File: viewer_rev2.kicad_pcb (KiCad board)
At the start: 2 copper layers, 98 x 98 mm, 147 parts, among them J1 USB_C_Receptacle_PowerOnly_6P, Q1 DMG3414U, SW1 SW_SPDT, U1 TLC555xD

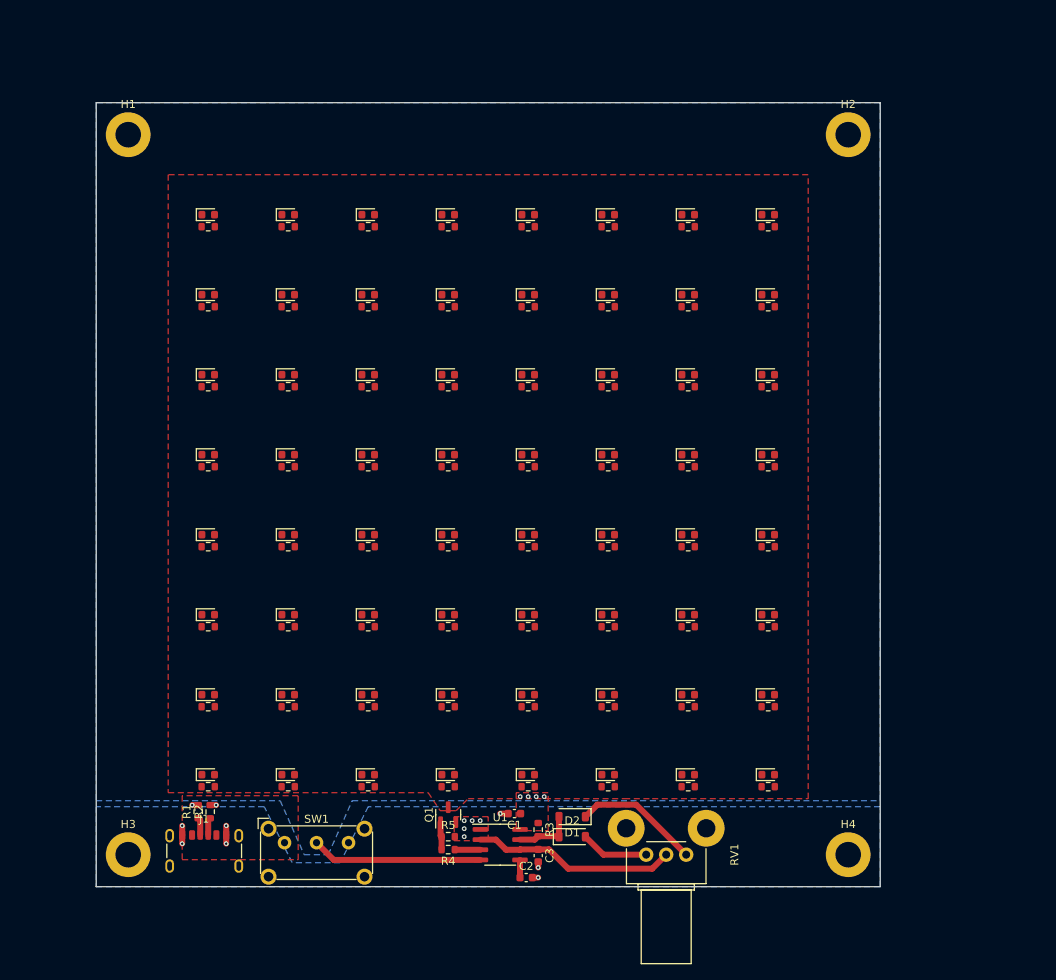
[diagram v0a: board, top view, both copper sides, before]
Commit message: Draft version for 96 well plate
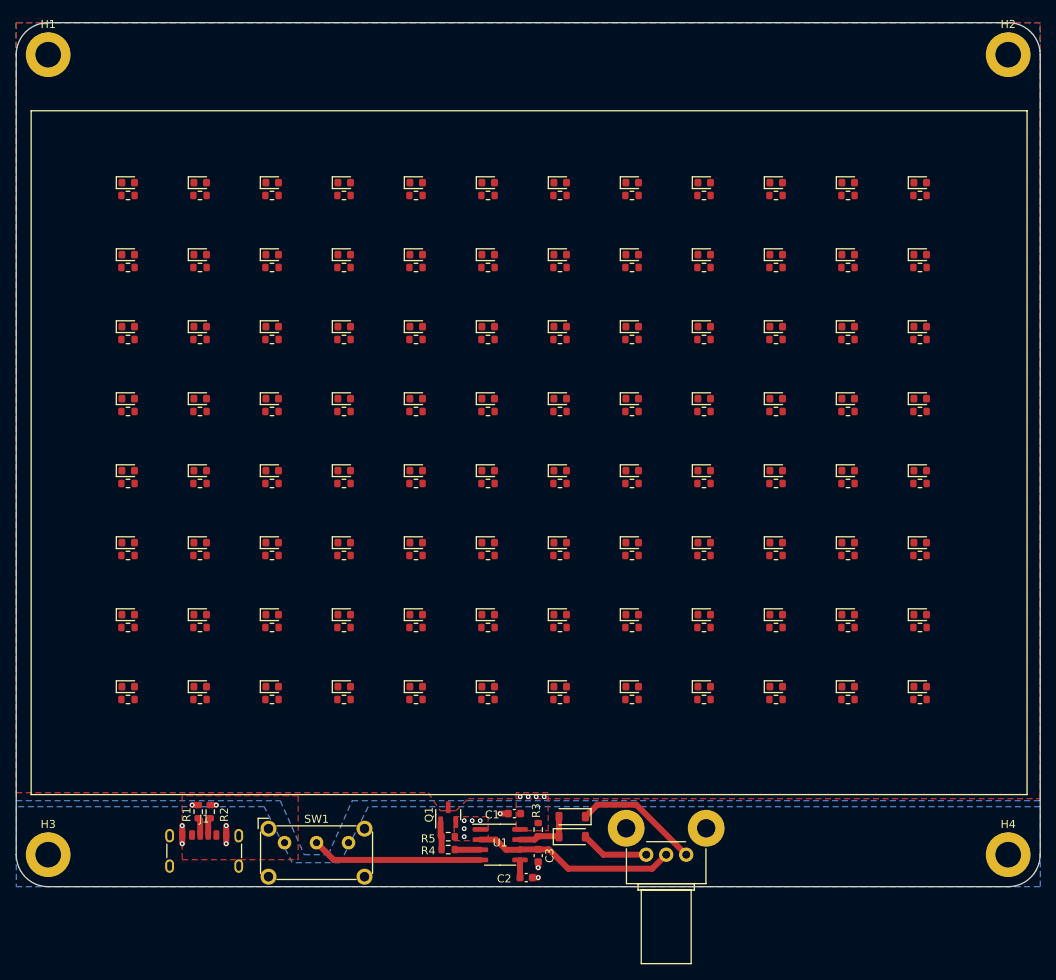
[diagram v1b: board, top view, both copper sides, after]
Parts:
- added D67: LED, LED_SMD:LED_0603_1608Metric, F.Cu at (153.5, 94.0)
- added D68: LED, LED_SMD:LED_0603_1608Metric, F.Cu at (162.5, 94.0)
- added D69: LED, LED_SMD:LED_0603_1608Metric, F.Cu at (171.5, 94.0)
- added D70: LED, LED_SMD:LED_0603_1608Metric, F.Cu at (180.5, 94.0)
- added D71: LED, LED_SMD:LED_0603_1608Metric, F.Cu at (189.5, 94.0)
- added D72: LED, LED_SMD:LED_0603_1608Metric, F.Cu at (198.5, 94.0)
- added D73: LED, LED_SMD:LED_0603_1608Metric, F.Cu at (207.5, 94.0)
- added D74: LED, LED_SMD:LED_0603_1608Metric, F.Cu at (216.5, 94.0)
- added D75: LED, LED_SMD:LED_0603_1608Metric, F.Cu at (117.5, 103.0)
- added D76: LED, LED_SMD:LED_0603_1608Metric, F.Cu at (126.5, 103.0)
- added D77: LED, LED_SMD:LED_0603_1608Metric, F.Cu at (135.5, 103.0)
- added D78: LED, LED_SMD:LED_0603_1608Metric, F.Cu at (144.5, 103.0)
- added D79: LED, LED_SMD:LED_0603_1608Metric, F.Cu at (153.5, 103.0)
- added D80: LED, LED_SMD:LED_0603_1608Metric, F.Cu at (162.5, 103.0)
- added D81: LED, LED_SMD:LED_0603_1608Metric, F.Cu at (171.5, 103.0)
- added D82: LED, LED_SMD:LED_0603_1608Metric, F.Cu at (180.5, 103.0)
- added D83: LED, LED_SMD:LED_0603_1608Metric, F.Cu at (189.5, 103.0)
- added D84: LED, LED_SMD:LED_0603_1608Metric, F.Cu at (198.5, 103.0)
- added D85: LED, LED_SMD:LED_0603_1608Metric, F.Cu at (207.5, 103.0)
- added D86: LED, LED_SMD:LED_0603_1608Metric, F.Cu at (216.5, 103.0)
- added D87: LED, LED_SMD:LED_0603_1608Metric, F.Cu at (117.5, 112.0)
- added D88: LED, LED_SMD:LED_0603_1608Metric, F.Cu at (126.5, 112.0)
- added D89: LED, LED_SMD:LED_0603_1608Metric, F.Cu at (135.5, 112.0)
- added D90: LED, LED_SMD:LED_0603_1608Metric, F.Cu at (144.5, 112.0)
- added D91: LED, LED_SMD:LED_0603_1608Metric, F.Cu at (153.5, 112.0)
- added D92: LED, LED_SMD:LED_0603_1608Metric, F.Cu at (162.5, 112.0)
- added D93: LED, LED_SMD:LED_0603_1608Metric, F.Cu at (171.5, 112.0)
- added D94: LED, LED_SMD:LED_0603_1608Metric, F.Cu at (180.5, 112.0)
- added D95: LED, LED_SMD:LED_0603_1608Metric, F.Cu at (189.5, 112.0)
- added D96: LED, LED_SMD:LED_0603_1608Metric, F.Cu at (198.5, 112.0)
- added D97: LED, LED_SMD:LED_0603_1608Metric, F.Cu at (207.5, 112.0)
- added D98: LED, LED_SMD:LED_0603_1608Metric, F.Cu at (216.5, 112.0)
- added R100: 91, Resistor_SMD:R_0603_1608Metric, F.Cu at (207.5, 113.6)
- added R101: 91, Resistor_SMD:R_0603_1608Metric, F.Cu at (216.5, 113.6)
- added R70: 91, Resistor_SMD:R_0603_1608Metric, F.Cu at (153.5, 95.6)
- added R71: 91, Resistor_SMD:R_0603_1608Metric, F.Cu at (162.5, 95.6)
- added R72: 91, Resistor_SMD:R_0603_1608Metric, F.Cu at (171.5, 95.6)
- added R73: 91, Resistor_SMD:R_0603_1608Metric, F.Cu at (180.5, 95.6)
- added R74: 91, Resistor_SMD:R_0603_1608Metric, F.Cu at (189.5, 95.6)
- added R75: 91, Resistor_SMD:R_0603_1608Metric, F.Cu at (198.5, 95.6)
- added R76: 91, Resistor_SMD:R_0603_1608Metric, F.Cu at (207.5, 95.6)
- added R77: 91, Resistor_SMD:R_0603_1608Metric, F.Cu at (216.5, 95.6)
- added R78: 91, Resistor_SMD:R_0603_1608Metric, F.Cu at (117.5, 104.6)
- added R79: 91, Resistor_SMD:R_0603_1608Metric, F.Cu at (126.5, 104.6)
- added R80: 91, Resistor_SMD:R_0603_1608Metric, F.Cu at (135.5, 104.6)
- added R81: 91, Resistor_SMD:R_0603_1608Metric, F.Cu at (144.5, 104.6)
- added R82: 91, Resistor_SMD:R_0603_1608Metric, F.Cu at (153.5, 104.6)
- added R83: 91, Resistor_SMD:R_0603_1608Metric, F.Cu at (162.5, 104.6)
- added R84: 91, Resistor_SMD:R_0603_1608Metric, F.Cu at (171.5, 104.6)
- added R85: 91, Resistor_SMD:R_0603_1608Metric, F.Cu at (180.5, 104.6)
- added R86: 91, Resistor_SMD:R_0603_1608Metric, F.Cu at (189.5, 104.6)
- added R87: 91, Resistor_SMD:R_0603_1608Metric, F.Cu at (198.5, 104.6)
- added R88: 91, Resistor_SMD:R_0603_1608Metric, F.Cu at (207.5, 104.6)
- added R89: 91, Resistor_SMD:R_0603_1608Metric, F.Cu at (216.5, 104.6)
- added R90: 91, Resistor_SMD:R_0603_1608Metric, F.Cu at (117.5, 113.6)
- added R91: 91, Resistor_SMD:R_0603_1608Metric, F.Cu at (126.5, 113.6)
- added R92: 91, Resistor_SMD:R_0603_1608Metric, F.Cu at (135.5, 113.6)
- added R93: 91, Resistor_SMD:R_0603_1608Metric, F.Cu at (144.5, 113.6)
- added R94: 91, Resistor_SMD:R_0603_1608Metric, F.Cu at (153.5, 113.6)
- added R95: 91, Resistor_SMD:R_0603_1608Metric, F.Cu at (162.5, 113.6)
- added R96: 91, Resistor_SMD:R_0603_1608Metric, F.Cu at (171.5, 113.6)
- added R97: 91, Resistor_SMD:R_0603_1608Metric, F.Cu at (180.5, 113.6)
- added R98: 91, Resistor_SMD:R_0603_1608Metric, F.Cu at (189.5, 113.6)
- added R99: 91, Resistor_SMD:R_0603_1608Metric, F.Cu at (198.5, 113.6)
- R10, R11, R12, R13, R14, R15, R16, R17, R18, R19, R20, R21, R22, R23, R24, R25, R26, R27, R28, R29, R30, R31, R32, R33, R34, R35, R36, R37, R38, R39, R40, R41, R42, R43, R44, R45, R46, R47, R48, R49, R50, R51, R52, R53, R54, R55, R56, R57, R58, R59, R6, R60, R61, R62, R63, R64, R65, R66, R67, R68, R69, R7, R8, R9: value 68 -> 91
- moved D59 72.7 mm to (189.5, 85.0)
- moved R62 72.6 mm to (189.5, 86.6)
- moved D60 71.9 mm to (198.5, 85.0)
- moved R63 71.8 mm to (198.5, 86.6)
- moved D61 71.0 mm to (207.5, 85.0)
- moved R64 70.9 mm to (207.5, 86.6)
- moved D62 70.2 mm to (216.5, 85.0)
- moved R65 70.1 mm to (216.5, 86.6)
- moved D35 67.2 mm to (189.5, 67.0)
- moved R38 67.2 mm to (189.5, 68.6)
- moved D36 66.3 mm to (198.5, 67.0)
- moved R39 66.2 mm to (198.5, 68.6)
- moved D37 65.4 mm to (207.5, 67.0)
- moved R40 65.3 mm to (207.5, 68.6)
- moved D38 64.5 mm to (216.5, 67.0)
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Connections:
- D10 pad 2: Net-(D10-A) -> Net-(D3-A)
- D11 pad 2: Net-(D11-A) -> Net-(D3-A)
- D12 pad 2: Net-(D12-A) -> Net-(D3-A)
- D13 pad 2: Net-(D13-A) -> Net-(D3-A)
- D14 pad 2: Net-(D14-A) -> Net-(D3-A)
- D15 pad 2: Net-(D15-A) -> Net-(D3-A)
- D16 pad 2: Net-(D16-A) -> Net-(D3-A)
- D17 pad 2: Net-(D17-A) -> Net-(D3-A)
- D18 pad 2: Net-(D18-A) -> Net-(D3-A)
- D19 pad 2: Net-(D19-A) -> Net-(D3-A)
- D20 pad 2: Net-(D20-A) -> Net-(D3-A)
- D21 pad 2: Net-(D21-A) -> Net-(D3-A)
- D22 pad 2: Net-(D22-A) -> Net-(D3-A)
- D23 pad 2: Net-(D23-A) -> Net-(D3-A)
- D24 pad 2: Net-(D24-A) -> Net-(D3-A)
- D25 pad 2: Net-(D25-A) -> Net-(D3-A)
- D26 pad 2: Net-(D26-A) -> Net-(D3-A)
- D27 pad 2: Net-(D27-A) -> Net-(D3-A)
- D28 pad 2: Net-(D28-A) -> Net-(D3-A)
- D29 pad 2: Net-(D29-A) -> Net-(D3-A)
- D30 pad 2: Net-(D30-A) -> Net-(D3-A)
- D31 pad 2: Net-(D31-A) -> Net-(D3-A)
- D32 pad 2: Net-(D32-A) -> Net-(D3-A)
- D33 pad 2: Net-(D33-A) -> Net-(D3-A)
- D34 pad 2: Net-(D34-A) -> Net-(D3-A)
- D35 pad 2: Net-(D35-A) -> Net-(D3-A)
- D36 pad 2: Net-(D36-A) -> Net-(D3-A)
- D37 pad 2: Net-(D37-A) -> Net-(D3-A)
- D38 pad 2: Net-(D38-A) -> Net-(D3-A)
- D39 pad 2: Net-(D39-A) -> Net-(D3-A)
- D4 pad 2: Net-(D4-A) -> Net-(D3-A)
- D40 pad 2: Net-(D40-A) -> Net-(D3-A)
- D41 pad 2: Net-(D41-A) -> Net-(D3-A)
- D42 pad 2: Net-(D42-A) -> Net-(D3-A)
- D43 pad 2: Net-(D43-A) -> Net-(D3-A)
- D44 pad 2: Net-(D44-A) -> Net-(D3-A)
- D45 pad 2: Net-(D45-A) -> Net-(D3-A)
- D46 pad 2: Net-(D46-A) -> Net-(D3-A)
- D47 pad 2: Net-(D47-A) -> Net-(D3-A)
- D48 pad 2: Net-(D48-A) -> Net-(D3-A)
- D49 pad 2: Net-(D49-A) -> Net-(D3-A)
- D5 pad 2: Net-(D5-A) -> Net-(D3-A)
- D50 pad 2: Net-(D50-A) -> Net-(D3-A)
- D51 pad 2: Net-(D51-A) -> Net-(D3-A)
- D52 pad 2: Net-(D52-A) -> Net-(D3-A)
- D53 pad 2: Net-(D53-A) -> Net-(D3-A)
- D54 pad 2: Net-(D54-A) -> Net-(D3-A)
- D55 pad 2: Net-(D55-A) -> Net-(D3-A)
- D56 pad 2: Net-(D56-A) -> Net-(D3-A)
- D57 pad 2: Net-(D57-A) -> Net-(D3-A)
- D58 pad 2: Net-(D58-A) -> Net-(D3-A)
- D59 pad 2: Net-(D59-A) -> Net-(D3-A)
- D6 pad 2: Net-(D6-A) -> Net-(D3-A)
- D60 pad 2: Net-(D60-A) -> Net-(D3-A)
- D61 pad 2: Net-(D61-A) -> Net-(D3-A)
- D62 pad 2: Net-(D62-A) -> Net-(D3-A)
- D63 pad 2: Net-(D63-A) -> Net-(D3-A)
- D64 pad 2: Net-(D64-A) -> Net-(D3-A)
- D65 pad 2: Net-(D65-A) -> Net-(D3-A)
- D66 pad 2: Net-(D66-A) -> Net-(D3-A)
- D7 pad 2: Net-(D7-A) -> Net-(D3-A)
- D8 pad 2: Net-(D8-A) -> Net-(D3-A)
- D9 pad 2: Net-(D9-A) -> Net-(D3-A)
- R10 pad 2: Net-(D7-A) -> Net-(D3-A)
- R11 pad 2: Net-(D8-A) -> Net-(D3-A)
- R12 pad 2: Net-(D9-A) -> Net-(D3-A)
- R13 pad 2: Net-(D10-A) -> Net-(D3-A)
- R14 pad 2: Net-(D11-A) -> Net-(D3-A)
- R15 pad 2: Net-(D12-A) -> Net-(D3-A)
- R16 pad 2: Net-(D13-A) -> Net-(D3-A)
- R17 pad 2: Net-(D14-A) -> Net-(D3-A)
- R18 pad 2: Net-(D15-A) -> Net-(D3-A)
- R19 pad 2: Net-(D16-A) -> Net-(D3-A)
- R20 pad 2: Net-(D17-A) -> Net-(D3-A)
- R21 pad 2: Net-(D18-A) -> Net-(D3-A)
- R22 pad 2: Net-(D19-A) -> Net-(D3-A)
- R23 pad 2: Net-(D20-A) -> Net-(D3-A)
- R24 pad 2: Net-(D21-A) -> Net-(D3-A)
- R25 pad 2: Net-(D22-A) -> Net-(D3-A)
- R26 pad 2: Net-(D23-A) -> Net-(D3-A)
- R27 pad 2: Net-(D24-A) -> Net-(D3-A)
- R28 pad 2: Net-(D25-A) -> Net-(D3-A)
- R29 pad 2: Net-(D26-A) -> Net-(D3-A)
- R30 pad 2: Net-(D27-A) -> Net-(D3-A)
- R31 pad 2: Net-(D28-A) -> Net-(D3-A)
- R32 pad 2: Net-(D29-A) -> Net-(D3-A)
- R33 pad 2: Net-(D30-A) -> Net-(D3-A)
- R34 pad 2: Net-(D31-A) -> Net-(D3-A)
- R35 pad 2: Net-(D32-A) -> Net-(D3-A)
- R36 pad 2: Net-(D33-A) -> Net-(D3-A)
- R37 pad 2: Net-(D34-A) -> Net-(D3-A)
- R38 pad 2: Net-(D35-A) -> Net-(D3-A)
- R39 pad 2: Net-(D36-A) -> Net-(D3-A)
- R40 pad 2: Net-(D37-A) -> Net-(D3-A)
- R41 pad 2: Net-(D38-A) -> Net-(D3-A)
- R42 pad 2: Net-(D39-A) -> Net-(D3-A)
- R43 pad 2: Net-(D40-A) -> Net-(D3-A)
- R44 pad 2: Net-(D41-A) -> Net-(D3-A)
- R45 pad 2: Net-(D42-A) -> Net-(D3-A)
- R46 pad 2: Net-(D43-A) -> Net-(D3-A)
- R47 pad 2: Net-(D44-A) -> Net-(D3-A)
- R48 pad 2: Net-(D45-A) -> Net-(D3-A)
- R49 pad 2: Net-(D46-A) -> Net-(D3-A)
- R50 pad 2: Net-(D47-A) -> Net-(D3-A)
- R51 pad 2: Net-(D48-A) -> Net-(D3-A)
- R52 pad 2: Net-(D49-A) -> Net-(D3-A)
- R53 pad 2: Net-(D50-A) -> Net-(D3-A)
- R54 pad 2: Net-(D51-A) -> Net-(D3-A)
- R55 pad 2: Net-(D52-A) -> Net-(D3-A)
- R56 pad 2: Net-(D53-A) -> Net-(D3-A)
- R57 pad 2: Net-(D54-A) -> Net-(D3-A)
- R58 pad 2: Net-(D55-A) -> Net-(D3-A)
- R59 pad 2: Net-(D56-A) -> Net-(D3-A)
- R60 pad 2: Net-(D57-A) -> Net-(D3-A)
- R61 pad 2: Net-(D58-A) -> Net-(D3-A)
- R62 pad 2: Net-(D59-A) -> Net-(D3-A)
- R63 pad 2: Net-(D60-A) -> Net-(D3-A)
- R64 pad 2: Net-(D61-A) -> Net-(D3-A)
- R65 pad 2: Net-(D62-A) -> Net-(D3-A)
- R66 pad 2: Net-(D63-A) -> Net-(D3-A)
- R67 pad 2: Net-(D64-A) -> Net-(D3-A)
- R68 pad 2: Net-(D65-A) -> Net-(D3-A)
- R69 pad 2: Net-(D66-A) -> Net-(D3-A)
- R7 pad 2: Net-(D4-A) -> Net-(D3-A)
- R8 pad 2: Net-(D5-A) -> Net-(D3-A)
- R9 pad 2: Net-(D6-A) -> Net-(D3-A)
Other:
- board size 98 x 98 mm -> 128 x 108 mm

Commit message: update USB-C conn and add JLC PNs
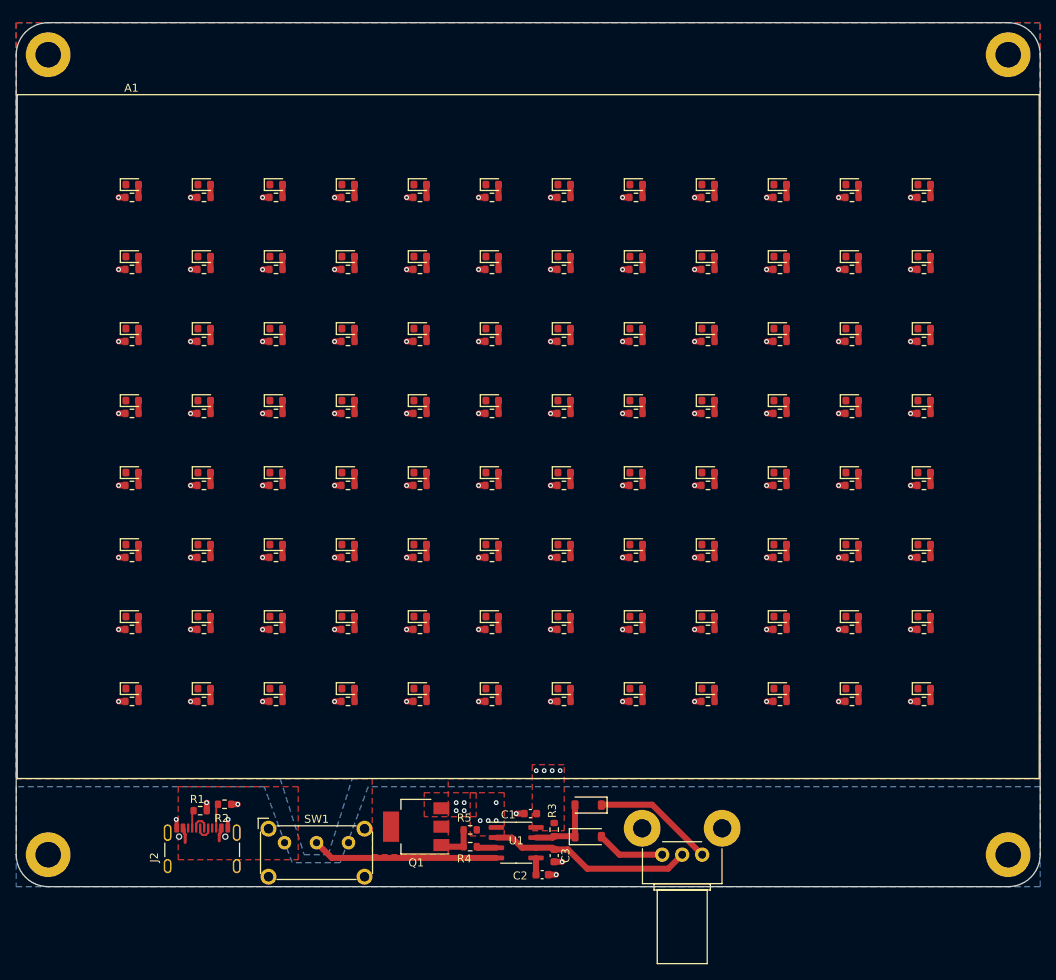
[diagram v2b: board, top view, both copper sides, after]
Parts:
- removed J1: USB_C_Receptacle_PowerOnly_6P, Connector_USB:USB_C_Receptacle_GCT_USB4125-xx-x_6P_TopMnt_Horizontal
- added J2: USB_C_Receptacle_USB2.0_16P, Connector_USB:USB_C_Receptacle_GCT_USB4105-xx-A_16P_TopMnt_Horizontal, F.Cu at (126.8, 133.3)
- Q1: value DMG3414U -> ZXMN4A06GTA; footprint Package_TO_SOT_SMD:SOT-23 -> Package_TO_SOT_SMD:SOT-223-3_TabPin2
- moved Q1 4.27 mm to (153.5, 129.5), turned to 180 degrees
- moved R5 2.88 mm to (160.2, 129.9)
- moved R4 2.77 mm to (160.2, 132.0)
- moved D1 2.47 mm to (175.0, 126.8)
- moved C2 2.03 mm to (169.2, 135.5)
- moved R2 2.02 mm to (129.6, 126.7), turned to 0 degrees
- moved U1 2.02 mm to (166.0, 131.5)
- moved C1 2.00 mm to (167.8, 127.9)
- moved C3 2.00 mm to (170.8, 133.1)
- moved D2 2.00 mm to (175.0, 130.8)
- moved R3 2.00 mm to (170.8, 129.9)
- moved RV1 2.00 mm to (184.2, 133.0)
- moved R100 0.55 mm to (208.0, 113.8)
- moved R101 0.55 mm to (217.0, 113.8)
- moved R30 0.55 mm to (118.0, 68.8)
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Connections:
- D10 pad 2: Net-(D3-A) -> Net-(D10-A)
- D11 pad 2: Net-(D3-A) -> Net-(D11-A)
- D12 pad 2: Net-(D3-A) -> Net-(D12-A)
- D13 pad 2: Net-(D3-A) -> Net-(D13-A)
- D14 pad 2: Net-(D3-A) -> Net-(D14-A)
- D15 pad 2: Net-(D3-A) -> Net-(D15-A)
- D16 pad 2: Net-(D3-A) -> Net-(D16-A)
- D17 pad 2: Net-(D3-A) -> Net-(D17-A)
- D18 pad 2: Net-(D3-A) -> Net-(D18-A)
- D19 pad 2: Net-(D3-A) -> Net-(D19-A)
- D20 pad 2: Net-(D3-A) -> Net-(D20-A)
- D21 pad 2: Net-(D3-A) -> Net-(D21-A)
- D22 pad 2: Net-(D3-A) -> Net-(D22-A)
- D23 pad 2: Net-(D3-A) -> Net-(D23-A)
- D24 pad 2: Net-(D3-A) -> Net-(D24-A)
- D25 pad 2: Net-(D3-A) -> Net-(D25-A)
- D26 pad 2: Net-(D3-A) -> Net-(D26-A)
- D27 pad 2: Net-(D3-A) -> Net-(D27-A)
- D28 pad 2: Net-(D3-A) -> Net-(D28-A)
- D29 pad 2: Net-(D3-A) -> Net-(D29-A)
- D30 pad 2: Net-(D3-A) -> Net-(D30-A)
- D31 pad 2: Net-(D3-A) -> Net-(D31-A)
- D32 pad 2: Net-(D3-A) -> Net-(D32-A)
- D33 pad 2: Net-(D3-A) -> Net-(D33-A)
- D34 pad 2: Net-(D3-A) -> Net-(D34-A)
- D35 pad 2: Net-(D3-A) -> Net-(D35-A)
- D36 pad 2: Net-(D3-A) -> Net-(D36-A)
- D37 pad 2: Net-(D3-A) -> Net-(D37-A)
- D38 pad 2: Net-(D3-A) -> Net-(D38-A)
- D39 pad 2: Net-(D3-A) -> Net-(D39-A)
- D4 pad 2: Net-(D3-A) -> Net-(D4-A)
- D40 pad 2: Net-(D3-A) -> Net-(D40-A)
- D41 pad 2: Net-(D3-A) -> Net-(D41-A)
- D42 pad 2: Net-(D3-A) -> Net-(D42-A)
- D43 pad 2: Net-(D3-A) -> Net-(D43-A)
- D44 pad 2: Net-(D3-A) -> Net-(D44-A)
- D45 pad 2: Net-(D3-A) -> Net-(D45-A)
- D46 pad 2: Net-(D3-A) -> Net-(D46-A)
- D47 pad 2: Net-(D3-A) -> Net-(D47-A)
- D48 pad 2: Net-(D3-A) -> Net-(D48-A)
- D49 pad 2: Net-(D3-A) -> Net-(D49-A)
- D5 pad 2: Net-(D3-A) -> Net-(D5-A)
- D50 pad 2: Net-(D3-A) -> Net-(D50-A)
- D51 pad 2: Net-(D3-A) -> Net-(D51-A)
- D52 pad 2: Net-(D3-A) -> Net-(D52-A)
- D53 pad 2: Net-(D3-A) -> Net-(D53-A)
- D54 pad 2: Net-(D3-A) -> Net-(D54-A)
- D55 pad 2: Net-(D3-A) -> Net-(D55-A)
- D56 pad 2: Net-(D3-A) -> Net-(D56-A)
- D57 pad 2: Net-(D3-A) -> Net-(D57-A)
- D58 pad 2: Net-(D3-A) -> Net-(D58-A)
- D59 pad 2: Net-(D3-A) -> Net-(D59-A)
- D6 pad 2: Net-(D3-A) -> Net-(D6-A)
- D60 pad 2: Net-(D3-A) -> Net-(D60-A)
- D61 pad 2: Net-(D3-A) -> Net-(D61-A)
- D62 pad 2: Net-(D3-A) -> Net-(D62-A)
- D63 pad 2: Net-(D3-A) -> Net-(D63-A)
- D64 pad 2: Net-(D3-A) -> Net-(D64-A)
- D65 pad 2: Net-(D3-A) -> Net-(D65-A)
- D66 pad 2: Net-(D3-A) -> Net-(D66-A)
- D67 pad 2: Net-(D3-A) -> Net-(D67-A)
- D68 pad 2: Net-(D3-A) -> Net-(D68-A)
- D69 pad 2: Net-(D3-A) -> Net-(D69-A)
- D7 pad 2: Net-(D3-A) -> Net-(D7-A)
- D70 pad 2: Net-(D3-A) -> Net-(D70-A)
- D71 pad 2: Net-(D3-A) -> Net-(D71-A)
- D72 pad 2: Net-(D3-A) -> Net-(D72-A)
- D73 pad 2: Net-(D3-A) -> Net-(D73-A)
- D74 pad 2: Net-(D3-A) -> Net-(D74-A)
- D75 pad 2: Net-(D3-A) -> Net-(D75-A)
- D76 pad 2: Net-(D3-A) -> Net-(D76-A)
- D77 pad 2: Net-(D3-A) -> Net-(D77-A)
- D78 pad 2: Net-(D3-A) -> Net-(D78-A)
- D79 pad 2: Net-(D3-A) -> Net-(D79-A)
- D8 pad 2: Net-(D3-A) -> Net-(D8-A)
- D80 pad 2: Net-(D3-A) -> Net-(D80-A)
- D81 pad 2: Net-(D3-A) -> Net-(D81-A)
- D82 pad 2: Net-(D3-A) -> Net-(D82-A)
- D83 pad 2: Net-(D3-A) -> Net-(D83-A)
- D84 pad 2: Net-(D3-A) -> Net-(D84-A)
- D85 pad 2: Net-(D3-A) -> Net-(D85-A)
- D86 pad 2: Net-(D3-A) -> Net-(D86-A)
- D87 pad 2: Net-(D3-A) -> Net-(D87-A)
- D88 pad 2: Net-(D3-A) -> Net-(D88-A)
- D89 pad 2: Net-(D3-A) -> Net-(D89-A)
- D9 pad 2: Net-(D3-A) -> Net-(D9-A)
- D90 pad 2: Net-(D3-A) -> Net-(D90-A)
- D91 pad 2: Net-(D3-A) -> Net-(D91-A)
- D92 pad 2: Net-(D3-A) -> Net-(D92-A)
- D93 pad 2: Net-(D3-A) -> Net-(D93-A)
- D94 pad 2: Net-(D3-A) -> Net-(D94-A)
- D95 pad 2: Net-(D3-A) -> Net-(D95-A)
- D96 pad 2: Net-(D3-A) -> Net-(D96-A)
- D97 pad 2: Net-(D3-A) -> Net-(D97-A)
- D98 pad 2: Net-(D3-A) -> Net-(D98-A)
- Q1 pad 2: GND -> NMOS_DRAIN
- Q1 pad 3: NMOS_DRAIN -> GND
- R10 pad 2: Net-(D3-A) -> Net-(D7-A)
- R100 pad 2: Net-(D3-A) -> Net-(D97-A)
- R101 pad 2: Net-(D3-A) -> Net-(D98-A)
- R11 pad 2: Net-(D3-A) -> Net-(D8-A)
- R12 pad 2: Net-(D3-A) -> Net-(D9-A)
- R13 pad 2: Net-(D3-A) -> Net-(D10-A)
- R14 pad 2: Net-(D3-A) -> Net-(D11-A)
- R15 pad 2: Net-(D3-A) -> Net-(D12-A)
- R16 pad 2: Net-(D3-A) -> Net-(D13-A)
- R17 pad 2: Net-(D3-A) -> Net-(D14-A)
- R18 pad 2: Net-(D3-A) -> Net-(D15-A)
- R19 pad 2: Net-(D3-A) -> Net-(D16-A)
- R20 pad 2: Net-(D3-A) -> Net-(D17-A)
- R21 pad 2: Net-(D3-A) -> Net-(D18-A)
- R22 pad 2: Net-(D3-A) -> Net-(D19-A)
- R23 pad 2: Net-(D3-A) -> Net-(D20-A)
- R24 pad 2: Net-(D3-A) -> Net-(D21-A)
- R25 pad 2: Net-(D3-A) -> Net-(D22-A)
- R26 pad 2: Net-(D3-A) -> Net-(D23-A)
- R27 pad 2: Net-(D3-A) -> Net-(D24-A)
- R28 pad 2: Net-(D3-A) -> Net-(D25-A)
- R29 pad 2: Net-(D3-A) -> Net-(D26-A)
- R30 pad 2: Net-(D3-A) -> Net-(D27-A)
- R31 pad 2: Net-(D3-A) -> Net-(D28-A)
- R32 pad 2: Net-(D3-A) -> Net-(D29-A)
- R33 pad 2: Net-(D3-A) -> Net-(D30-A)
- R34 pad 2: Net-(D3-A) -> Net-(D31-A)
- R35 pad 2: Net-(D3-A) -> Net-(D32-A)
- R36 pad 2: Net-(D3-A) -> Net-(D33-A)
- R37 pad 2: Net-(D3-A) -> Net-(D34-A)
- R38 pad 2: Net-(D3-A) -> Net-(D35-A)
- R39 pad 2: Net-(D3-A) -> Net-(D36-A)
- R40 pad 2: Net-(D3-A) -> Net-(D37-A)
- R41 pad 2: Net-(D3-A) -> Net-(D38-A)
- R42 pad 2: Net-(D3-A) -> Net-(D39-A)
- R43 pad 2: Net-(D3-A) -> Net-(D40-A)
- R44 pad 2: Net-(D3-A) -> Net-(D41-A)
- R45 pad 2: Net-(D3-A) -> Net-(D42-A)
- R46 pad 2: Net-(D3-A) -> Net-(D43-A)
- R47 pad 2: Net-(D3-A) -> Net-(D44-A)
- R48 pad 2: Net-(D3-A) -> Net-(D45-A)
- R49 pad 2: Net-(D3-A) -> Net-(D46-A)
- R50 pad 2: Net-(D3-A) -> Net-(D47-A)
- R51 pad 2: Net-(D3-A) -> Net-(D48-A)
- R52 pad 2: Net-(D3-A) -> Net-(D49-A)
- R53 pad 2: Net-(D3-A) -> Net-(D50-A)
- R54 pad 2: Net-(D3-A) -> Net-(D51-A)
- R55 pad 2: Net-(D3-A) -> Net-(D52-A)
- R56 pad 2: Net-(D3-A) -> Net-(D53-A)
- R57 pad 2: Net-(D3-A) -> Net-(D54-A)
- R58 pad 2: Net-(D3-A) -> Net-(D55-A)
- R59 pad 2: Net-(D3-A) -> Net-(D56-A)
- R60 pad 2: Net-(D3-A) -> Net-(D57-A)
- R61 pad 2: Net-(D3-A) -> Net-(D58-A)
- R62 pad 2: Net-(D3-A) -> Net-(D59-A)
- R63 pad 2: Net-(D3-A) -> Net-(D60-A)
- R64 pad 2: Net-(D3-A) -> Net-(D61-A)
- R65 pad 2: Net-(D3-A) -> Net-(D62-A)
- R66 pad 2: Net-(D3-A) -> Net-(D63-A)
- R67 pad 2: Net-(D3-A) -> Net-(D64-A)
- R68 pad 2: Net-(D3-A) -> Net-(D65-A)
- R69 pad 2: Net-(D3-A) -> Net-(D66-A)
- R7 pad 2: Net-(D3-A) -> Net-(D4-A)
- R70 pad 2: Net-(D3-A) -> Net-(D67-A)
- R71 pad 2: Net-(D3-A) -> Net-(D68-A)
- R72 pad 2: Net-(D3-A) -> Net-(D69-A)
- R73 pad 2: Net-(D3-A) -> Net-(D70-A)
- R74 pad 2: Net-(D3-A) -> Net-(D71-A)
- R75 pad 2: Net-(D3-A) -> Net-(D72-A)
- R76 pad 2: Net-(D3-A) -> Net-(D73-A)
- R77 pad 2: Net-(D3-A) -> Net-(D74-A)
- R78 pad 2: Net-(D3-A) -> Net-(D75-A)
- R79 pad 2: Net-(D3-A) -> Net-(D76-A)
- R8 pad 2: Net-(D3-A) -> Net-(D5-A)
- R80 pad 2: Net-(D3-A) -> Net-(D77-A)
- R81 pad 2: Net-(D3-A) -> Net-(D78-A)
- R82 pad 2: Net-(D3-A) -> Net-(D79-A)
- R83 pad 2: Net-(D3-A) -> Net-(D80-A)
- R84 pad 2: Net-(D3-A) -> Net-(D81-A)
- R85 pad 2: Net-(D3-A) -> Net-(D82-A)
- R86 pad 2: Net-(D3-A) -> Net-(D83-A)
- R87 pad 2: Net-(D3-A) -> Net-(D84-A)
- R88 pad 2: Net-(D3-A) -> Net-(D85-A)
- R89 pad 2: Net-(D3-A) -> Net-(D86-A)
- R9 pad 2: Net-(D3-A) -> Net-(D6-A)
- R90 pad 2: Net-(D3-A) -> Net-(D87-A)
- R91 pad 2: Net-(D3-A) -> Net-(D88-A)
- R92 pad 2: Net-(D3-A) -> Net-(D89-A)
- R93 pad 2: Net-(D3-A) -> Net-(D90-A)
- R94 pad 2: Net-(D3-A) -> Net-(D91-A)
- R95 pad 2: Net-(D3-A) -> Net-(D92-A)
- R96 pad 2: Net-(D3-A) -> Net-(D93-A)
- R97 pad 2: Net-(D3-A) -> Net-(D94-A)
- R98 pad 2: Net-(D3-A) -> Net-(D95-A)
- R99 pad 2: Net-(D3-A) -> Net-(D96-A)
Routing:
- net VCC: track 21.4 -> 103.9 mm, vias 4 -> 100
- net Net-(SW1-A): track 0.00 -> 3.64 mm
- net Net-(J2-D+-PadA6): track 0.00 -> 2.38 mm
- net Net-(J2-D--PadA7): track 0.00 -> 2.38 mm
- net Net-(D3-A): track 0.00 -> 1.61 mm
- net Net-(D98-A): track 0.00 -> 1.59 mm
- net Net-(D97-A): track 0.00 -> 1.59 mm
- net Net-(D96-A): track 0.00 -> 1.59 mm
- net Net-(D95-A): track 0.00 -> 1.59 mm
- net Net-(D94-A): track 0.00 -> 1.59 mm
- net Net-(D93-A): track 0.00 -> 1.59 mm
- net Net-(D92-A): track 0.00 -> 1.59 mm
- net Net-(D91-A): track 0.00 -> 1.59 mm
- net Net-(D90-A): track 0.00 -> 1.59 mm
- net Net-(D89-A): track 0.00 -> 1.59 mm
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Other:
- board text added: "A1"

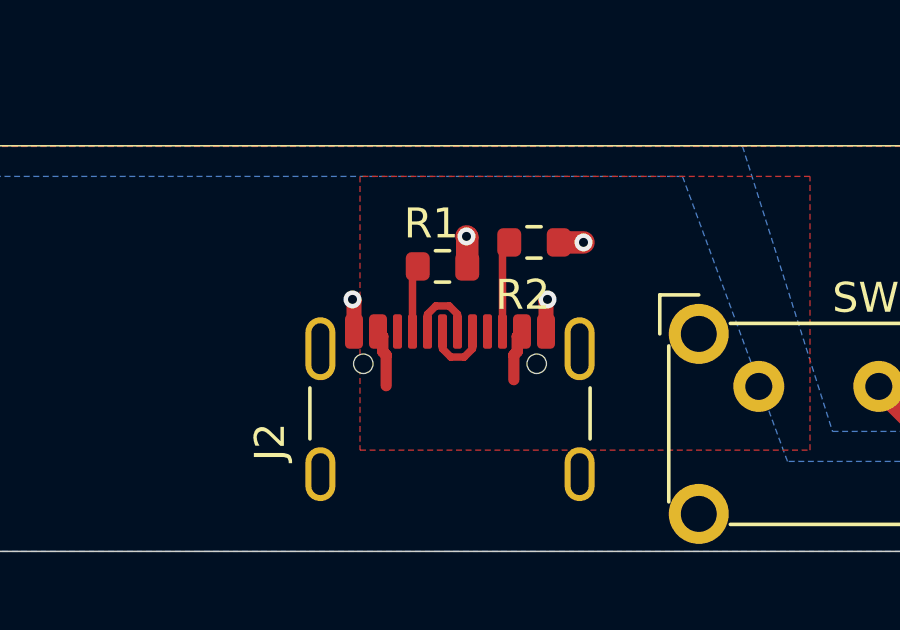
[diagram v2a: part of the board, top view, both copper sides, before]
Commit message: Modify clearance setting and change to fit. Other changes to satisfy ERC / DRC
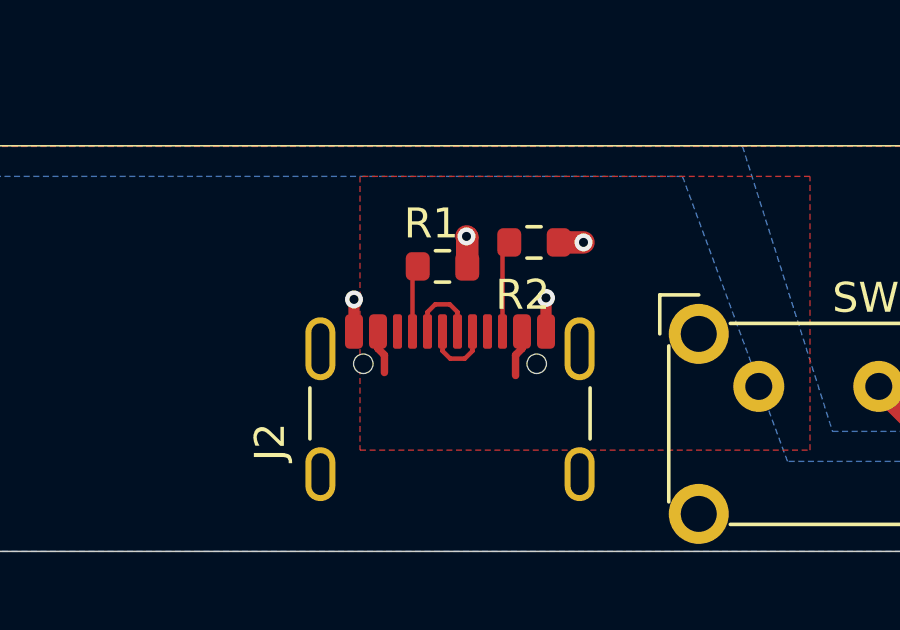
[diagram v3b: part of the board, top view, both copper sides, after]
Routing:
- net Net-(SW1-A): track 3.64 -> 3.01 mm
